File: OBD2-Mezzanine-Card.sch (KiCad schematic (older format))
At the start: 2 parts, among them P1 CONN_02X20

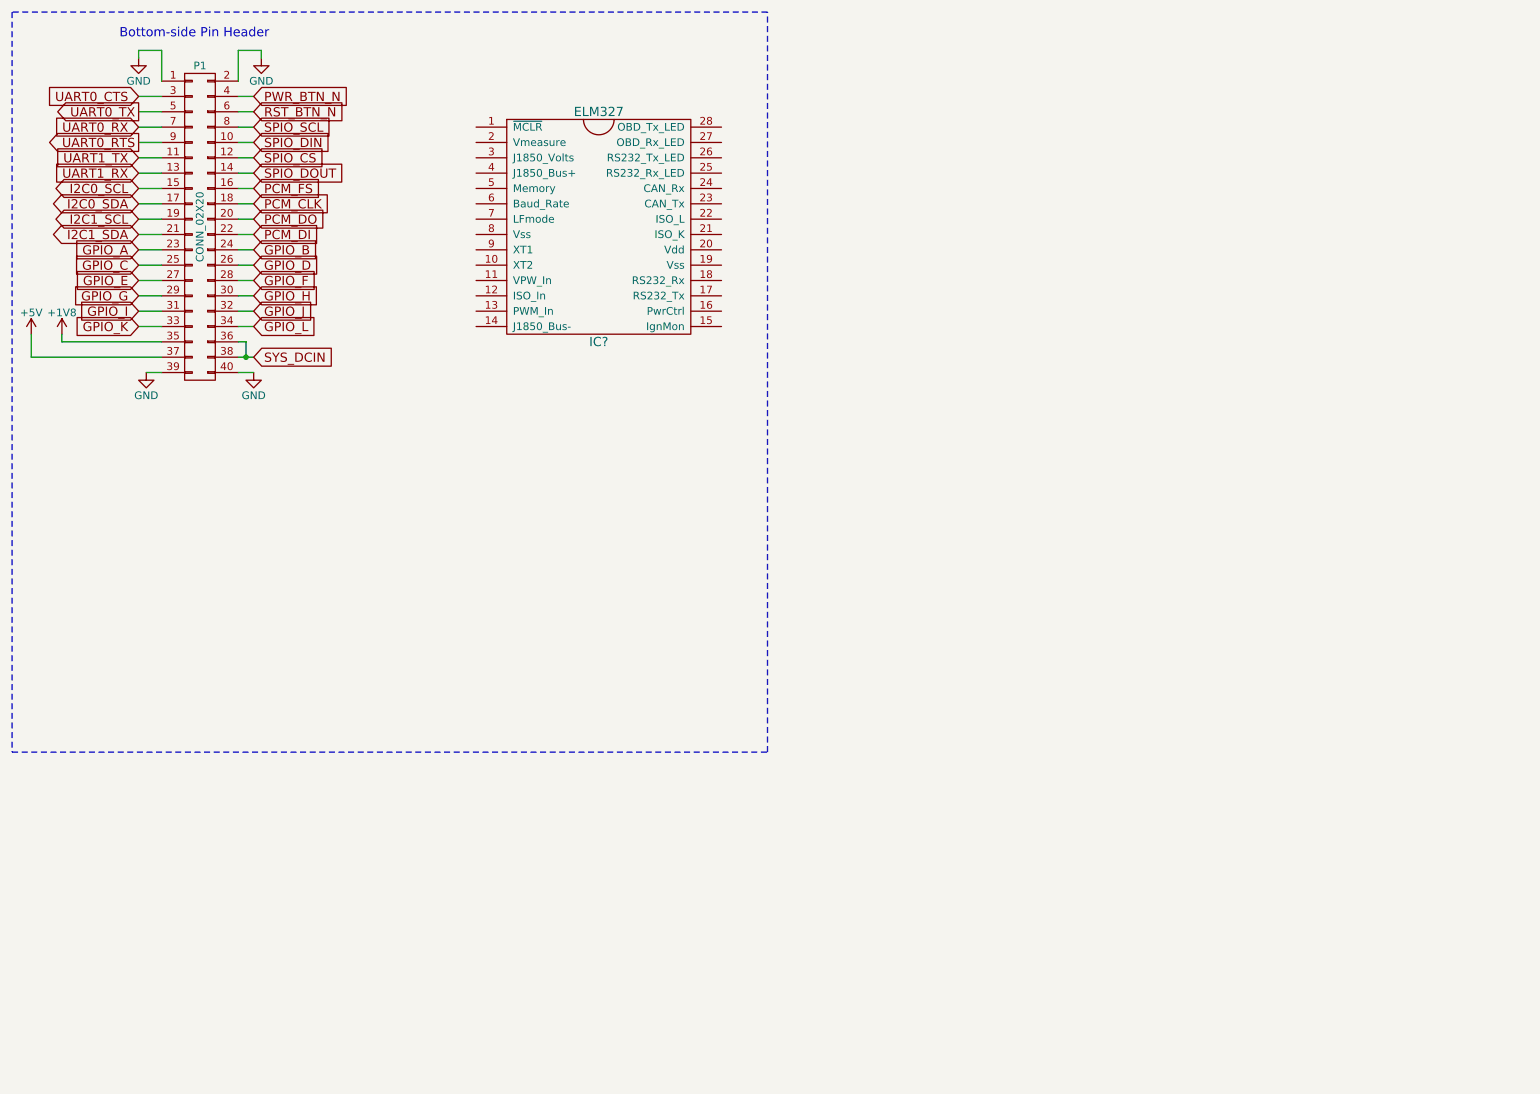
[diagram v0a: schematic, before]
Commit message: sch: Connect the Light Emitting Diodes
Signed-off-by: Alistair Francis <alistair@alistair23.me>
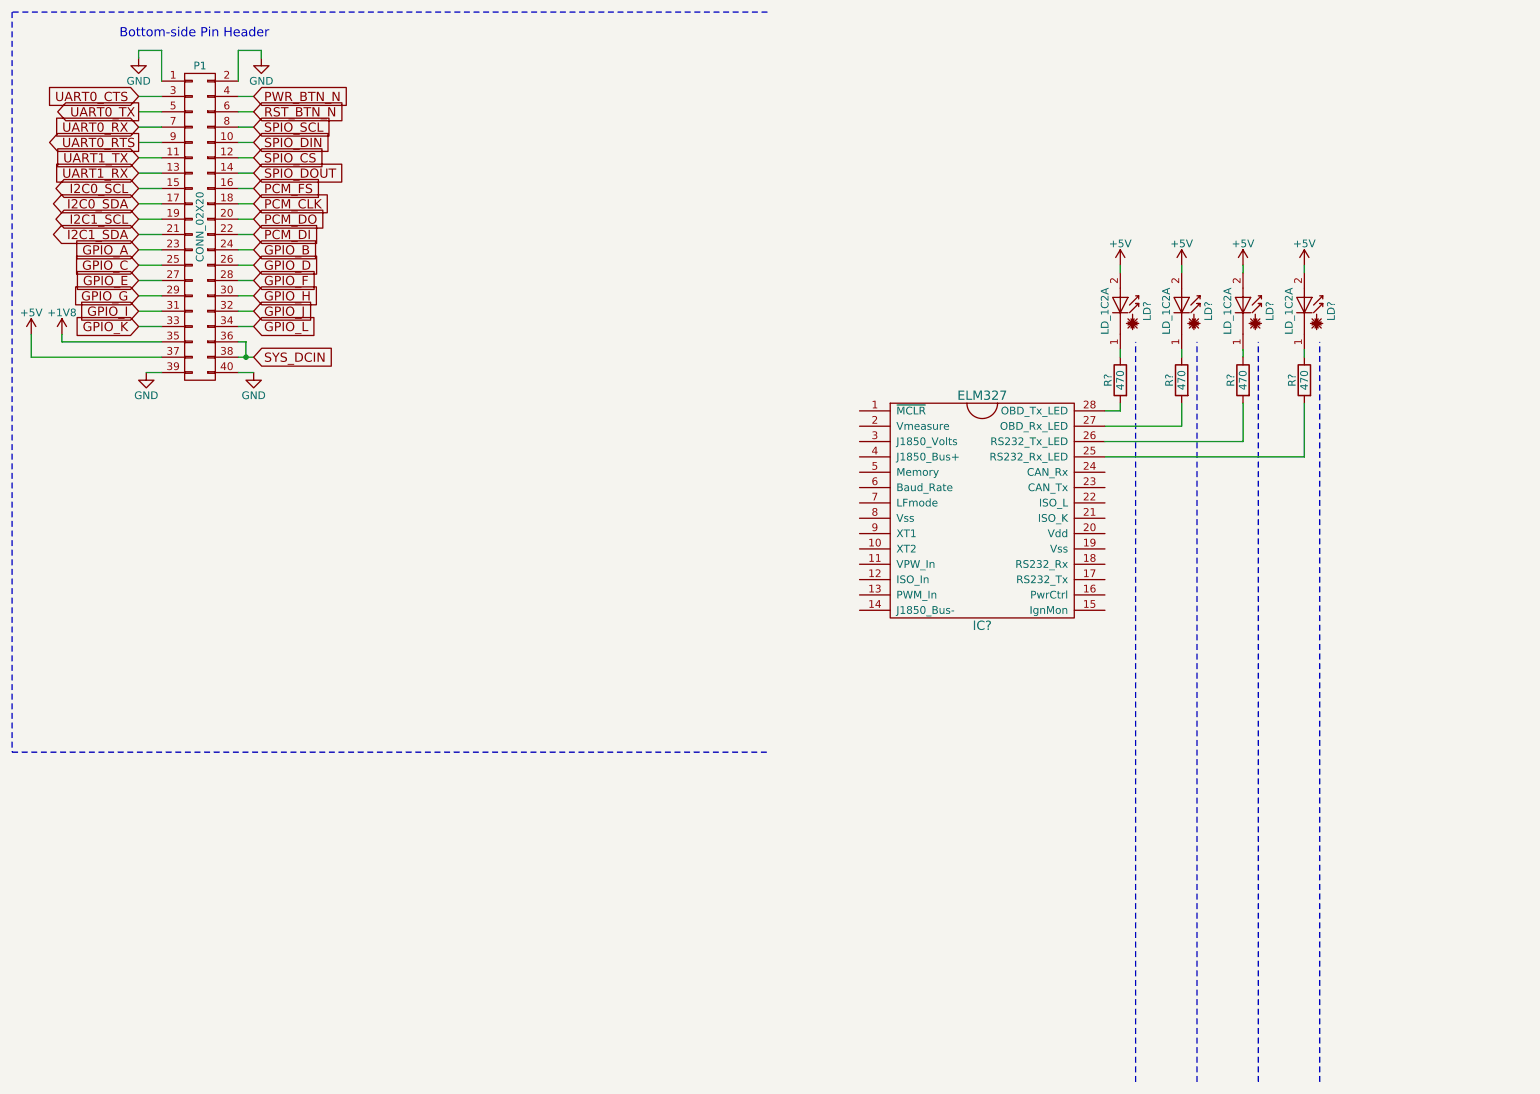
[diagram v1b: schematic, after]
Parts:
- added LD? (x4): LD_1C2A, symbol Laserdiode_1C2A
- added R? (x4): 470, symbol R
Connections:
- net +5V: now also LD?.2 (A), LD?.2 (A), LD?.2 (A), LD?.2 (A)
- net at IC?.25 (RS232_Rx_LED): now also R?.2
- net at IC?.26 (RS232_Tx_LED): now also R?.2
- net at IC?.27 (OBD_Rx_LED): now also R?.2
- net at IC?.28 (OBD_Tx_LED): now also R?.2
- new net: LD?.1 (K), R?.1 (x4)
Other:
- moved on the sheet: IC?
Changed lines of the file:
@@
 	2150 2800 2200 2800
 Wire Wire Line
-	2150 2900 2200 2900
-Wire Wire Line
-	2200 2900 2250 2900
+	2150 2900 2250 2900
 Wire Wire Line
 	1500 900  1500 950
@@
 	675  5475 5600 5475
 Wire Notes Line
-	5600 5475 5600 650
+	8000 7625 8000 2800
 Wire Notes Line
 	5600 650  675  650
@@
 L ELM327 IC?
 U 1 1 5AA5E7D4
-P 4500 2050
-F 0 "IC?" H 4500 1300 60  0000 C CNN
-F 1 "ELM327" H 4500 2800 60  0000 C CNN
-F 2 "" H 4500 2800 60  0001 C CNN
-F 3 "" H 4500 2800 60  0001 C CNN
-	1    4500 2050
+P 7000 3900
+F 0 "IC?" H 7000 3150 60  0000 C CNN
+F 1 "ELM327" H 7000 4650 60  0000 C CNN
+F 2 "" H 7000 4650 60  0001 C CNN
+F 3 "" H 7000 4650 60  0001 C CNN
+	1    7000 3900
 	1    0    0    -1
 $EndComp
+$Comp
+L +5V #PWR?
+U 1 1 5AA5EB98
+P 7900 2300
+F 0 "#PWR?" H 7900 2150 50  0001 C CNN
+F 1 "+5V" H 7900 2440 50  0000 C CNN
+F 2 "" H 7900 2300 50  0001 C CNN
+F 3 "" H 7900 2300 50  0001 C CNN
+	1    7900 2300
+	-1   0    0    -1
+$EndComp
+$Comp
+L Laserdiode_1C2A LD?
+U 1 1 5AA5EBB0
+P 7900 2550
+F 0 "LD?" H 7850 2725 50  0000 C CNN
+F 1 "LD_1C2A" H 7850 2450 50  0000 C CNN
+F 2 "" H 7800 2525 50  0001 C CNN
+F 3 "" H 7930 2350 50  0001 C CNN
+	1    7900 2550
+	0    1    -1   0
+$EndComp
+$Comp
+L R R?
+U 1 1 5AA5EC1E
+P 7900 3050
+F 0 "R?" V 7980 3050 50  0000 C CNN
+F 1 "470" V 7900 3050 50  0000 C CNN
+F 2 "" V 7830 3050 50  0001 C CNN
+F 3 "" H 7900 3050 50  0001 C CNN
+	1    7900 3050
+	-1   0    0    -1
+$EndComp
+Wire Wire Line
+	7800 3250 7900 3250
+Wire Wire Line
+	7900 3250 7900 3200
+Wire Wire Line
+	7900 2300 7900 2350
+Wire Wire Line
+	7900 2850 7900 2900
+Wire Notes Line
+	8400 7625 8400 2800
+$Comp
+L +5V #PWR?
+U 1 1 5AA5EED5
+P 8300 2300
+F 0 "#PWR?" H 8300 2150 50  0001 C CNN
+F 1 "+5V" H 8300 2440 50  0000 C CNN
+F 2 "" H 8300 2300 50  0001 C CNN
+F 3 "" H 8300 2300 50  0001 C CNN
+	1    8300 2300
+	-1   0    0    -1
+$EndComp
+$Comp
+L Laserdiode_1C2A LD?
+U 1 1 5AA5EEDB
+P 8300 2550
+F 0 "LD?" H 8250 2725 50  0000 C CNN
+F 1 "LD_1C2A" H 8250 2450 50  0000 C CNN
+F 2 "" H 8200 2525 50  0001 C CNN
+F 3 "" H 8330 2350 50  0001 C CNN
+	1    8300 2550
+	0    1    -1   0
+$EndComp
+$Comp
+L R R?
+U 1 1 5AA5EEE1
+P 8300 3050
+F 0 "R?" V 8380 3050 50  0000 C CNN
+F 1 "470" V 8300 3050 50  0000 C CNN
+F 2 "" V 8230 3050 50  0001 C CNN
+F 3 "" H 8300 3050 50  0001 C CNN
+	1    8300 3050
+	-1   0    0    -1
+$EndComp
+Wire Wire Line
+	8300 2300 8300 2350
+Wire Wire Line
+	8300 2850 8300 2900
+Wire Notes Line
+	8800 7625 8800 2800
+$Comp
+L +5V #PWR?
+U 1 1 5AA5EF2A
+P 8700 2300
+F 0 "#PWR?" H 8700 2150 50  0001 C CNN
+F 1 "+5V" H 8700 2440 50  0000 C CNN
+F 2 "" H 8700 2300 50  0001 C CNN
+F 3 "" H 8700 2300 50  0001 C CNN
+	1    8700 2300
+	-1   0    0    -1
+$EndComp
+$Comp
+L Laserdiode_1C2A LD?
+U 1 1 5AA5EF30
+P 8700 2550
+F 0 "LD?" H 8650 2725 50  0000 C CNN
+F 1 "LD_1C2A" H 8650 2450 50  0000 C CNN
+F 2 "" H 8600 2525 50  0001 C CNN
+F 3 "" H 8730 2350 50  0001 C CNN
+	1    8700 2550
+	0    1    -1   0
+$EndComp
+$Comp
+L R R?
+U 1 1 5AA5EF36
+P 8700 3050
+F 0 "R?" V 8780 3050 50  0000 C CNN
+F 1 "470" V 8700 3050 50  0000 C CNN
+F 2 "" V 8630 3050 50  0001 C CNN
+F 3 "" H 8700 3050 50  0001 C CNN
+	1    8700 3050
+	-1   0    0    -1
+$EndComp
+Wire Wire Line
+	8700 2300 8700 2350
+Wire Wire Line
+	8700 2850 8700 2900
+Wire Wire Line
+	7800 3350 8300 3350
+Wire Wire Line
+	8300 3350 8300 3200
+Wire Notes Line
+	9200 7625 9200 2800
+$Comp
+L +5V #PWR?
+U 1 1 5AA5EFD3
+P 9100 2300
+F 0 "#PWR?" H 9100 2150 50  0001 C CNN
+F 1 "+5V" H 9100 2440 50  0000 C CNN
+F 2 "" H 9100 2300 50  0001 C CNN
+F 3 "" H 9100 2300 50  0001 C CNN
+	1    9100 2300
+	-1   0    0    -1
+$EndComp
+$Comp
+L Laserdiode_1C2A LD?
+U 1 1 5AA5EFD9
+P 9100 2550
+F 0 "LD?" H 9050 2725 50  0000 C CNN
+F 1 "LD_1C2A" H 9050 2450 50  0000 C CNN
+F 2 "" H 9000 2525 50  0001 C CNN
+F 3 "" H 9130 2350 50  0001 C CNN
+	1    9100 2550
+	0    1    -1   0
+$EndComp
+$Comp
+L R R?
+U 1 1 5AA5EFDF
+P 9100 3050
+F 0 "R?" V 9180 3050 50  0000 C CNN
+F 1 "470" V 9100 3050 50  0000 C CNN
+F 2 "" V 9030 3050 50  0001 C CNN
+F 3 "" H 9100 3050 50  0001 C CNN
+	1    9100 3050
+	-1   0    0    -1
+$EndComp
+Wire Wire Line
+	9100 2300 9100 2350
+Wire Wire Line
+	9100 2850 9100 2900
+Wire Wire Line
+	7800 3450 8700 3450
+Wire Wire Line
+	8700 3450 8700 3200
+Wire Wire Line
+	7800 3550 9100 3550
+Wire Wire Line
+	9100 3550 9100 3200
 $EndSCHEMATC

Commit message: sch: Connect some of the power options
Signed-off-by: Alistair Francis <alistair@alistair23.me>
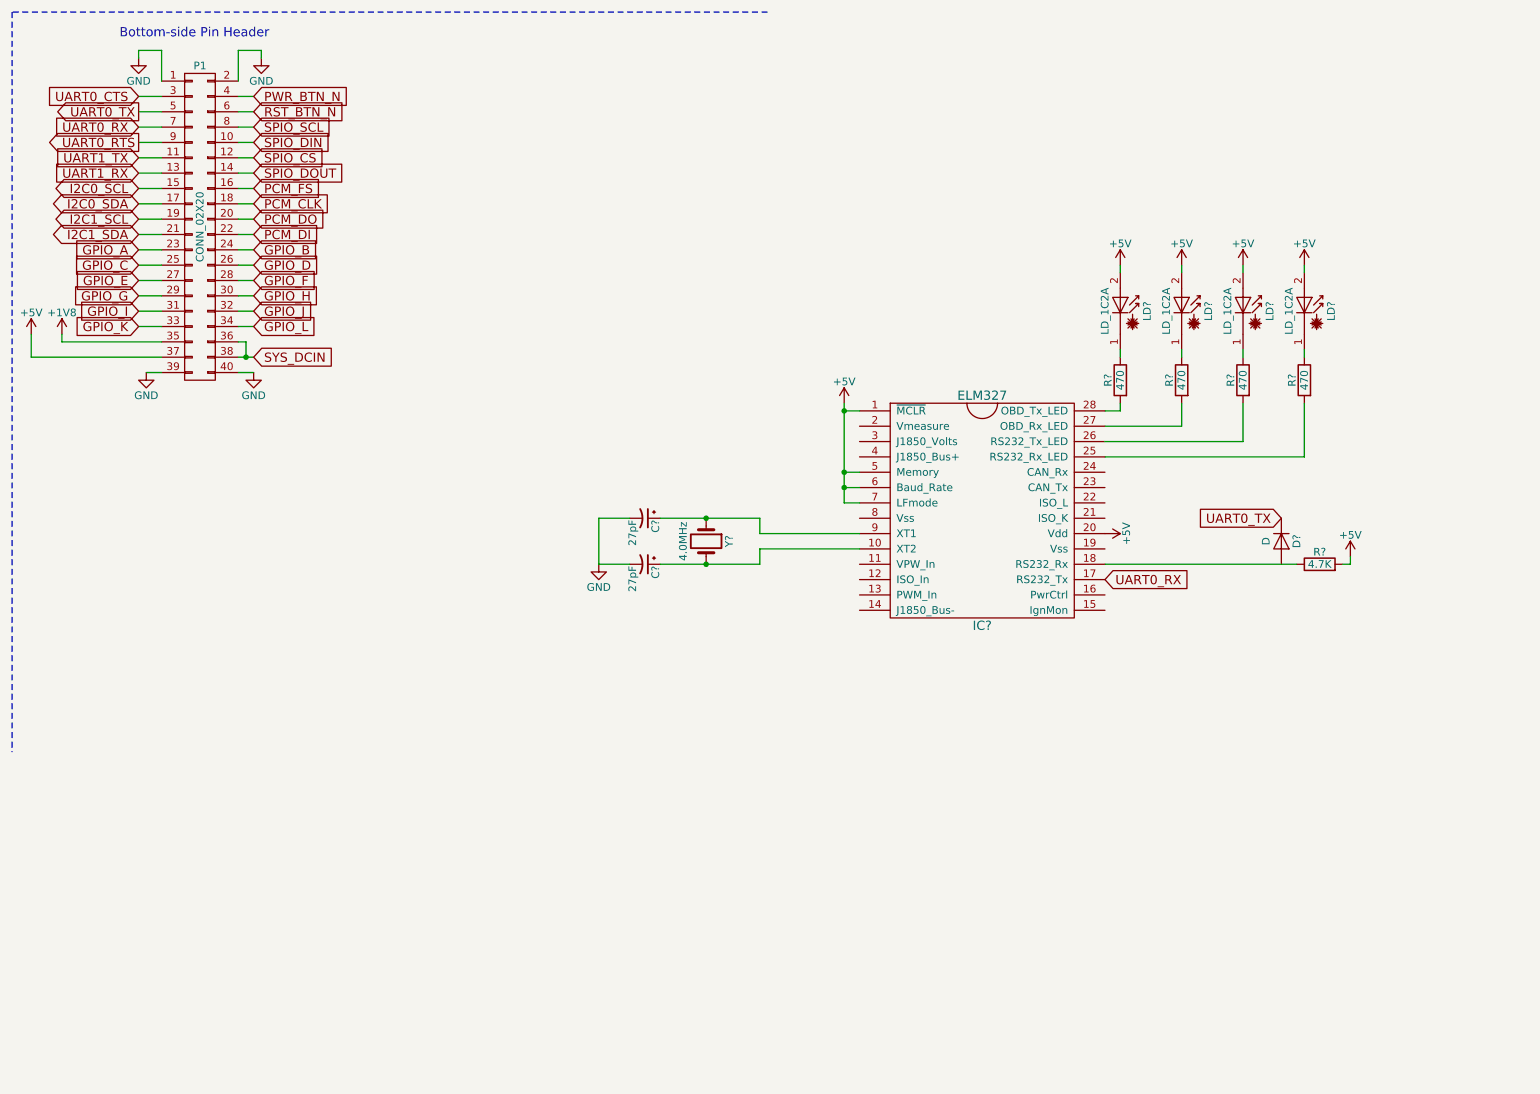
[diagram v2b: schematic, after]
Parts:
- added C? (x2): 27pF, symbol CP1_Small
- added D?: D, symbol D
- added R?: 4.7K, symbol R
- added Y?: 4.0MHz, symbol Crystal
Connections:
- net +5V: now also IC?.1 (~MCLR), IC?.20 (Vdd), IC?.5 (Memory), IC?.6 (Baud_Rate), IC?.7 (LFmode), R?.2
- net GND: now also C?.2, C?.2
- net UART0_RX: now also IC?.17 (RS232_Tx)
- net UART0_TX: now also D?.1 (K)
- net at IC?.10 (XT2): now also C?.1, Y?.2
- net at IC?.18 (RS232_Rx): now also R?.1
- net at IC?.9 (XT1): now also C?.1, Y?.1
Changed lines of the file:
@@
 	675  650  675  5475
-Wire Notes Line
-	675  5475 5600 5475
-Wire Notes Line
-	8000 7625 8000 2800
 Wire Notes Line
 	5600 650  675  650
@@
 Wire Wire Line
 	7900 2850 7900 2900
-Wire Notes Line
-	8400 7625 8400 2800
 $Comp
 L +5V #PWR?
@@
 Wire Wire Line
 	8300 2850 8300 2900
-Wire Notes Line
-	8800 7625 8800 2800
 $Comp
 L +5V #PWR?
@@
 Wire Wire Line
 	8300 3350 8300 3200
-Wire Notes Line
-	9200 7625 9200 2800
 $Comp
 L +5V #PWR?
@@
 Wire Wire Line
 	9100 3550 9100 3200
+$Comp
+L R R?
+U 1 1 5AA5F1D2
+P 9200 4250
+F 0 "R?" V 9280 4250 50  0000 C CNN
+F 1 "4.7K" V 9200 4250 50  0000 C CNN
+F 2 "" V 9130 4250 50  0001 C CNN
+F 3 "" H 9200 4250 50  0001 C CNN
+	1    9200 4250
+	0    -1   -1   0
+$EndComp
+$Comp
+L +5V #PWR?
+U 1 1 5AA5F31B
+P 9400 4200
+F 0 "#PWR?" H 9400 4050 50  0001 C CNN
+F 1 "+5V" H 9400 4340 50  0000 C CNN
+F 2 "" H 9400 4200 50  0001 C CNN
+F 3 "" H 9400 4200 50  0001 C CNN
+	1    9400 4200
+	1    0    0    -1
+$EndComp
+Wire Wire Line
+	7800 4250 9050 4250
+Wire Wire Line
+	9400 4250 9350 4250
+Wire Wire Line
+	9400 4200 9400 4250
+$Comp
+L D D?
+U 1 1 5AA5F5D5
+P 8950 4100
+F 0 "D?" H 8950 4200 50  0000 C CNN
+F 1 "D" H 8950 4000 50  0000 C CNN
+F 2 "" H 8950 4100 50  0001 C CNN
+F 3 "" H 8950 4100 50  0001 C CNN
+	1    8950 4100
+	0    1    1    0
+$EndComp
+Text GLabel 8950 3950 0    60   Input ~ 0
+UART0_TX
+Text GLabel 7800 4350 2    60   Input ~ 0
+UART0_RX
+$Comp
+L +5V #PWR?
+U 1 1 5AA60072
+P 7800 4050
+F 0 "#PWR?" H 7800 3900 50  0001 C CNN
+F 1 "+5V" H 7800 4190 50  0000 C CNN
+F 2 "" H 7800 4050 50  0001 C CNN
+F 3 "" H 7800 4050 50  0001 C CNN
+	1    7800 4050
+	0    1    1    0
+$EndComp
+$Comp
+L +5V #PWR?
+U 1 1 5AA601DB
+P 6100 3200
+F 0 "#PWR?" H 6100 3050 50  0001 C CNN
+F 1 "+5V" H 6100 3340 50  0000 C CNN
+F 2 "" H 6100 3200 50  0001 C CNN
+F 3 "" H 6100 3200 50  0001 C CNN
+	1    6100 3200
+	1    0    0    -1
+$EndComp
+Wire Wire Line
+	6200 3250 6100 3250
+Wire Wire Line
+	6100 3200 6100 3850
+Wire Wire Line
+	6100 3650 6200 3650
+Connection ~ 6100 3250
+Wire Wire Line
+	6100 3750 6200 3750
+Connection ~ 6100 3650
+Wire Wire Line
+	6100 3850 6200 3850
+Connection ~ 6100 3750
+$Comp
+L Crystal Y?
+U 1 1 5AA6110D
+P 5200 4100
+F 0 "Y?" H 5200 4250 50  0000 C CNN
+F 1 "4.0MHz" H 5200 3950 50  0000 C CNN
+F 2 "" H 5200 4100 50  0001 C CNN
+F 3 "" H 5200 4100 50  0001 C CNN
+	1    5200 4100
+	0    1    1    0
+$EndComp
+Wire Wire Line
+	4900 3950 5550 3950
+Wire Wire Line
+	5550 3950 5550 4050
+Wire Wire Line
+	5550 4050 6200 4050
+Wire Wire Line
+	6200 4150 5550 4150
+Wire Wire Line
+	5550 4250 5550 4150
+Wire Wire Line
+	4900 4250 5550 4250
+$Comp
+L CP1_Small C?
+U 1 1 5AA612FE
+P 4800 3950
+F 0 "C?" H 4810 4020 50  0000 L CNN
+F 1 "27pF" H 4810 3870 50  0000 L CNN
+F 2 "" H 4800 3950 50  0001 C CNN
+F 3 "" H 4800 3950 50  0001 C CNN
+	1    4800 3950
+	0    1    1    0
+$EndComp
+$Comp
+L CP1_Small C?
+U 1 1 5AA613D0
+P 4800 4250
+F 0 "C?" H 4810 4320 50  0000 L CNN
+F 1 "27pF" H 4810 4170 50  0000 L CNN
+F 2 "" H 4800 4250 50  0001 C CNN
+F 3 "" H 4800 4250 50  0001 C CNN
+	1    4800 4250
+	0    1    1    0
+$EndComp
+$Comp
+L GND #PWR?
+U 1 1 5AA613E7
+P 4500 4250
+F 0 "#PWR?" H 4500 4000 50  0001 C CNN
+F 1 "GND" H 4500 4100 50  0000 C CNN
+F 2 "" H 4500 4250 50  0001 C CNN
+F 3 "" H 4500 4250 50  0001 C CNN
+	1    4500 4250
+	1    0    0    -1
+$EndComp
+Connection ~ 5200 3950
+Wire Wire Line
+	4700 3950 4500 3950
+Wire Wire Line
+	4500 3950 4500 4250
+Wire Wire Line
+	4500 4250 4700 4250
+Connection ~ 5200 4250
 $EndSCHEMATC
